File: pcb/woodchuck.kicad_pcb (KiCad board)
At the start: 2 copper layers, 34 parts, among them IC1 24AA01, IC101 ADP3335, IC201 u-blox_CAM-M8Q, IC601 MS5611-01BA03, J401 JSTA-4, P101 CONN_01X02, P401 SWD, P402 USB_OTG, SW401 SPST, U301 Radiometrix_MTX2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

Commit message: regenerated and imported netlist
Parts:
- added C405: 1u, Woodchuck:C0603, F.Cu at (199.6, 122.6)
- added C406: 4u7, Woodchuck:C0603, F.Cu at (191.8, 117.4)
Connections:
- U401 pad 11: (no net) -> Net-(R401-Pad2)
- U401 pad 14: Net-(R401-Pad2) -> /Radio/MTX2_TXD
- U401 pad 28: /Radio/MTX2_TXD -> (no net)
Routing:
- net /Radio/MTX2_TXD: track 0.00 -> 8.23 mm
- net Net-(R401-Pad2): track 10.1 -> 1.88 mm
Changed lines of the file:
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@@
 (kicad_pcb (version 4) (host pcbnew 4.0.2-4+6225~38~ubuntu14.04.1-stable)
   (general
-    (links 133)
-    (no_connects 34)
-    (area 150 99.125 225.000001 137.579762)
+    (links 137)
+    (no_connects 39)
+    (area 0 0 0 0)
     (thickness 1.6)
     (drawings 5)
     (tracks 374)
     (zones 0)
-    (modules 34)
+    (modules 36)
     (nets 38)
   )
@@
       (net 3 +3V3))
     (pad 10 smd rect (at 1.75 4.25 90) (size 0.3 1.2) (layers F.Cu F.Paste F.Mask))
-    (pad 11 smd rect (at 2.25 4.25 90) (size 0.3 1.2) (layers F.Cu F.Paste F.Mask))
+    (pad 11 smd rect (at 2.25 4.25 90) (size 0.3 1.2) (layers F.Cu F.Paste F.Mask)
+      (net 29 "Net-(R401-Pad2)"))
     (pad 12 smd rect (at 2.75 4.25 90) (size 0.3 1.2) (layers F.Cu F.Paste F.Mask)
       (net 35 /GPS/GPS_FROM_MCU))
@@
       (net 34 /GPS/GPS_TO_MCU))
     (pad 14 smd rect (at 4.25 2.25 90) (size 1.2 0.3) (layers F.Cu F.Paste F.Mask)
-      (net 29 "Net-(R401-Pad2)"))
+      (net 9 /Radio/MTX2_TXD))
     (pad 15 smd rect (at 4.25 1.75 90) (size 1.2 0.3) (layers F.Cu F.Paste F.Mask)
       (net 31 "Net-(R402-Pad2)"))
@@
     (pad 27 smd rect (at 1.75 -4.25 90) (size 0.3 1.2) (layers F.Cu F.Paste F.Mask)
       (net 10 /Radio/MTX2_P1))
-    (pad 28 smd rect (at 1.25 -4.25 90) (size 0.3 1.2) (layers F.Cu F.Paste F.Mask)
-      (net 9 /Radio/MTX2_TXD))
+    (pad 28 smd rect (at 1.25 -4.25 90) (size 0.3 1.2) (layers F.Cu F.Paste F.Mask))
     (pad 29 smd rect (at 0.75 -4.25 90) (size 0.3 1.2) (layers F.Cu F.Paste F.Mask))
     (pad 30 smd rect (at 0.25 -4.25 90) (size 0.3 1.2) (layers F.Cu F.Paste F.Mask)
@@
     (pad 2 smd rect (at 1.7 0 270) (size 0.8 1.7) (layers F.Cu F.Paste F.Mask)
       (net 3 +3V3))
+  )
+  (module Woodchuck:C0603 (layer F.Cu)
+    (at 199.64 122.58 90)
+    (fp_text reference C405 (at 0.7 -1.35 90) (layer F.SilkS) hide
+      (effects (font (size 1 1) (thickness 0.15)))
+    )
+    (fp_text value 1u (at 0.75 1.45 90) (layer F.SilkS)
+      (effects (font (size 1 1) (thickness 0.15)))
+    )
+    (fp_line (start -0.4 0.5) (end 2 0.5) (layer F.SilkS) (width 0.15))
+    (fp_line (start -0.4 -0.5) (end 2 -0.5) (layer F.SilkS) (width 0.15))
+    (pad 1 smd rect (at 0 0 90) (size 0.8 0.8) (layers F.Cu F.Paste F.Mask)
+      (net 3 +3V3))
+    (pad 2 smd rect (at 1.6 0 90) (size 0.8 0.8) (layers F.Cu F.Paste F.Mask)
+      (net 1 GND))
+  )
+  (module Woodchuck:C0603 (layer F.Cu)
+    (at 191.84 117.39 90)
+    (fp_text reference C406 (at 0.7 -1.35 90) (layer F.SilkS) hide
+      (effects (font (size 1 1) (thickness 0.15)))
+    )
+    (fp_text value 4u7 (at 0.75 1.45 90) (layer F.SilkS)
+      (effects (font (size 1 1) (thickness 0.15)))
+    )
+    (fp_line (start -0.4 0.5) (end 2 0.5) (layer F.SilkS) (width 0.15))
+    (fp_line (start -0.4 -0.5) (end 2 -0.5) (layer F.SilkS) (width 0.15))
+    (pad 1 smd rect (at 0 0 90) (size 0.8 0.8) (layers F.Cu F.Paste F.Mask)
+      (net 3 +3V3))
+    (pad 2 smd rect (at 1.6 0 90) (size 0.8 0.8) (layers F.Cu F.Paste F.Mask)
+      (net 1 GND))
   )
   (gr_line (start 180 100.35) (end 180.05 100.35) (angle 90) (layer F.SilkS) (width 0.2))
@@
   (segment (start 203.85 126.4) (end 202.2 126.4) (width 0.3) (layer F.Cu) (net 7))
   (segment (start 204.7 125.55) (end 203.85 126.4) (width 0.3) (layer F.Cu) (net 7))
+  (segment (start 201.55 117.9) (end 201.25 117.9) (width 0.3) (layer F.Cu) (net 9))
+  (segment (start 199.15 116.85) (end 199.15 117.7) (width 0.3) (layer F.Cu) (net 9))
+  (segment (start 200.9 117.55) (end 200 116.65) (width 0.3) (layer F.Cu) (net 9))
+  (segment (start 200 116.65) (end 199.35 116.65) (width 0.3) (layer F.Cu) (net 9))
+  (segment (start 199.35 116.65) (end 199.15 116.85) (width 0.3) (layer F.Cu) (net 9))
+  (segment (start 201.25 117.9) (end 200.9 117.55) (width 0.3) (layer F.Cu) (net 9))
+  (segment (start 202.65 119) (end 201.55 117.9) (width 0.3) (layer F.Cu) (net 9))
+  (segment (start 204.65 121) (end 202.65 119) (width 0.3) (layer F.Cu) (net 9))
   (segment (start 195.65 117.7) (end 195.65 118.76) (width 0.3) (layer F.Cu) (net 13))
   (segment (start 214.83 119.96) (end 215.92 121.05) (width 0.3) (layer F.Cu) (net 13))
@@
   (segment (start 207.375 121.9) (end 209.275 121.9) (width 0.3) (layer F.Cu) (net 28))
   (segment (start 209.275 121.9) (end 209.5 121.675) (width 0.3) (layer F.Cu) (net 28))
-  (segment (start 201.55 117.9) (end 201.25 117.9) (width 0.3) (layer F.Cu) (net 29))
   (segment (start 204.65 121.4) (end 204.65 121) (width 0.3) (layer F.Cu) (net 29))
   (segment (start 205.15 121.9) (end 204.65 121.4) (width 0.3) (layer F.Cu) (net 29))
   (segment (start 205.925 121.9) (end 205.15 121.9) (width 0.3) (layer F.Cu) (net 29))
-  (segment (start 202.65 119) (end 201.55 117.9) (width 0.3) (layer F.Cu) (net 29))
-  (segment (start 204.65 121) (end 202.65 119) (width 0.3) (layer F.Cu) (net 29))
-  (segment (start 199.15 116.85) (end 199.15 117.7) (width 0.3) (layer F.Cu) (net 29))
-  (segment (start 200.9 117.55) (end 200 116.65) (width 0.3) (layer F.Cu) (net 29))
-  (segment (start 200 116.65) (end 199.35 116.65) (width 0.3) (layer F.Cu) (net 29))
-  (segment (start 199.35 116.65) (end 199.15 116.85) (width 0.3) (layer F.Cu) (net 29))
-  (segment (start 201.25 117.9) (end 200.9 117.55) (width 0.3) (layer F.Cu) (net 29))
   (segment (start 207.375 120.45) (end 207.975 120.45) (width 0.3) (layer F.Cu) (net 30))
   (segment (start 207.975 120.45) (end 209.5 118.925) (width 0.3) (layer F.Cu) (net 30))

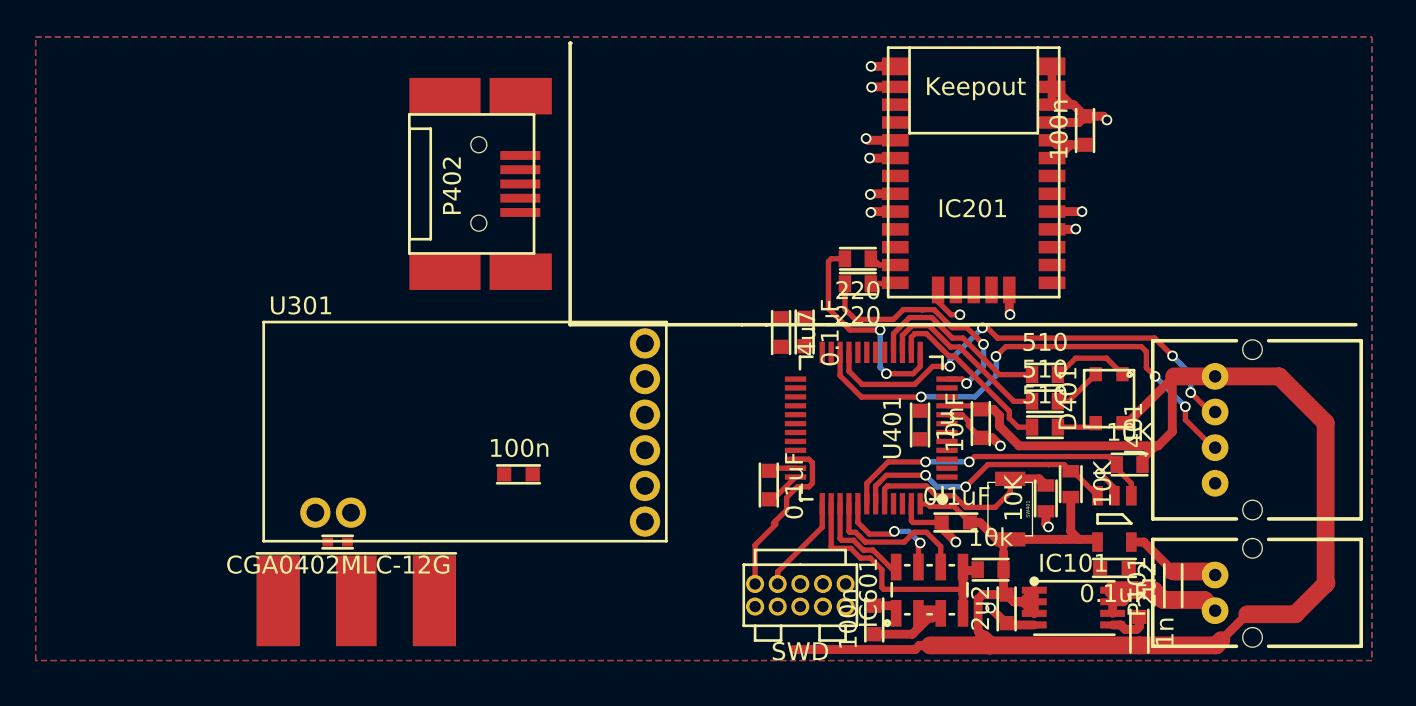
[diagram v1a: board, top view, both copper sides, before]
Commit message: PCB layout almost done. Add silkscreen and look over.
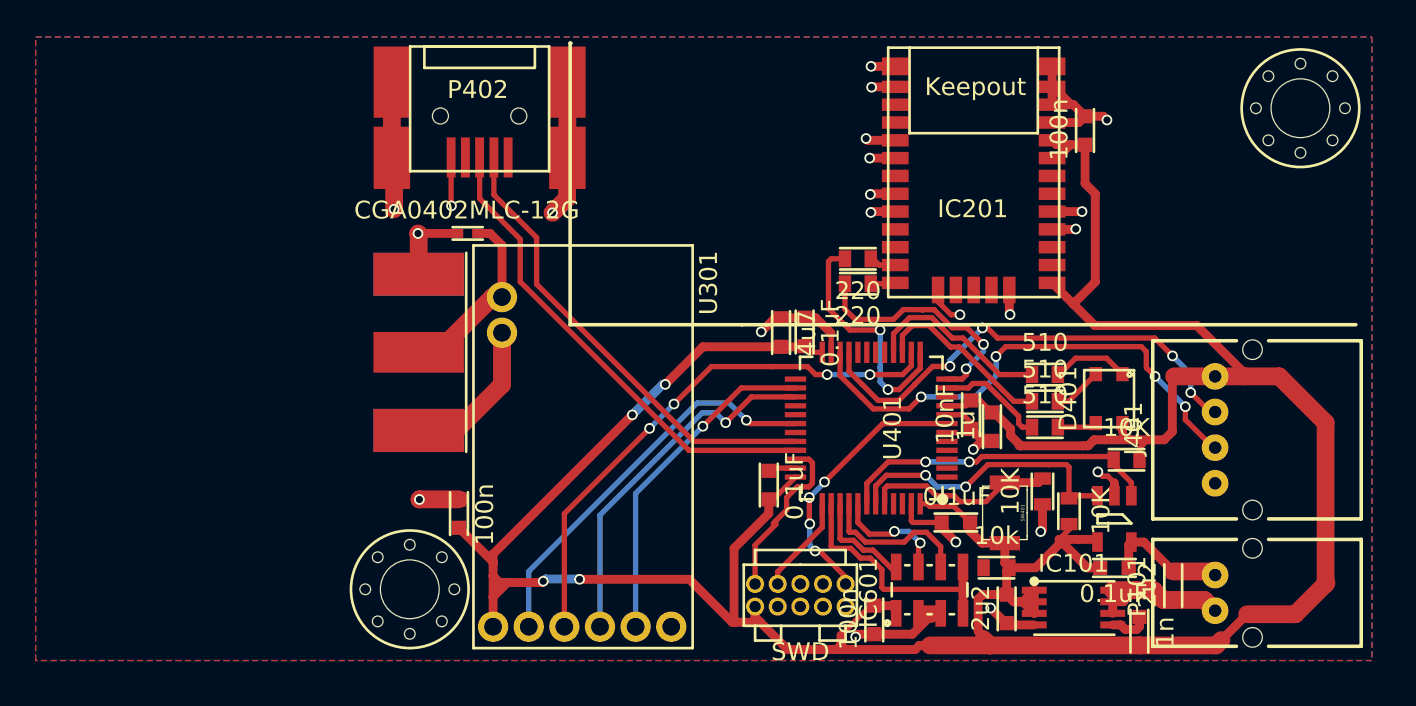
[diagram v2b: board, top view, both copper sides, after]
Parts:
- added X401: Mounting hole, Woodchuck:M3_MOUNT, F.Cu at (221.0, 104.0)
- added X402: Mounting hole, Woodchuck:M3_MOUNT, F.Cu at (171.0, 131.0)
- moved U301 20.4 mm to (174.6, 111.7), turned to 270 degrees
- moved D301 19.3 mm to (174.8, 111.0), turned to 180 degrees
- moved A301 14.4 mm to (171.5, 117.7), turned to 270 degrees
- moved C301 5.11 mm to (173.8, 127.5), turned to 90 degrees
- moved C405 4.31 mm to (203.7, 121.1), turned to 270 degrees
- moved R2 1.52 mm to (208.0, 126.6)
- moved C401 0.74 mm to (202.5, 120.4)
- moved P402 0.69 mm to (176.5, 106.8), turned to 270 degrees
- moved R404 0.43 mm to (206.5, 125.5)
- moved SW401 0.37 mm to (204.4, 126.7)
- moved R601 0.35 mm to (203.9, 129.8)
- moved R1 0.32 mm to (211.2, 123.7)
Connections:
- IC201 pad 2: (no net) -> Net-(IC201-Pad2)
- IC201 pad 28: (no net) -> Net-(IC201-Pad28)
- IC201 pad 29: (no net) -> Net-(IC201-Pad29)
- IC201 pad 3: (no net) -> Net-(IC201-Pad3)
- IC201 pad 30: (no net) -> Net-(IC201-Pad30)
- IC201 pad 6: (no net) -> Net-(IC201-Pad6)
- IC201 pad 7: (no net) -> Net-(IC201-Pad7)
- P401 pad 6: (no net) -> Net-(P401-Pad6)
- P401 pad 7: (no net) -> Net-(P401-Pad7)
- P401 pad 8: (no net) -> Net-(P401-Pad8)
- P402 pad 1: (no net) -> Net-(P402-Pad1)
- P402 pad 4: (no net) -> Net-(P402-Pad4)
- U401 pad 1: (no net) -> Net-(U401-Pad1)
- U401 pad 10: (no net) -> Net-(U401-Pad10)
- U401 pad 17: (no net) -> Net-(U401-Pad17)
- U401 pad 18: (no net) -> Net-(U401-Pad18)
- U401 pad 19: (no net) -> Net-(U401-Pad19)
- U401 pad 2: (no net) -> Net-(U401-Pad2)
- U401 pad 20: (no net) -> Net-(U401-Pad20)
- U401 pad 25: (no net) -> Net-(U401-Pad25)
- U401 pad 28: (no net) -> Net-(U401-Pad28)
- U401 pad 29: (no net) -> Net-(U401-Pad29)
- U401 pad 3: (no net) -> Net-(U401-Pad3)
- U401 pad 31: (no net) -> Net-(U401-Pad31)
- U401 pad 4: (no net) -> Net-(U401-Pad4)
- U401 pad 45: (no net) -> Net-(U401-Pad45)
- U401 pad 46: (no net) -> Net-(U401-Pad46)
- U401 pad 5: (no net) -> Net-(U401-Pad5)
- U401 pad 6: (no net) -> Net-(U401-Pad6)
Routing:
- net +3V3: track 107.3 -> 193.8 mm, vias 0 -> 4
- net GND: track 51.0 -> 94.1 mm, vias 16 -> 23
- net /microcontroller/USB_D+: track 0.00 -> 27.3 mm
- net /microcontroller/USB_D-: track 0.00 -> 26.3 mm
- net /Radio/MTX2_EN/PGM: track 0.00 -> 22.5 mm, vias 0 -> 1
- net /Radio/MTX2_TXD: track 8.23 -> 30.5 mm, vias 0 -> 4
- net /Radio/MTX2_P1: track 0.00 -> 20.4 mm, vias 0 -> 1
- net /Radio/MTX2_P0: track 0.00 -> 18.9 mm, vias 0 -> 1
- net /microcontroller/nRST: track 0.00 -> 15.3 mm, vias 0 -> 4
- net Net-(A301-Pad1): track 0.00 -> 10.5 mm
- net Net-(R401-Pad2): track 1.88 -> 6.13 mm
- net /GPS/GPS_TO_MCU: track 12.5 -> 13.8 mm
- net Net-(IC1-Pad3): track 15.3 -> 16.4 mm
- net /microcontroller/BOOT0: track 11.7 -> 10.7 mm
- net /barometer/BARO_CS: track 14.4 -> 13.6 mm
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
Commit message: Added logo and names to silk screen.
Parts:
- added X403: CUSF LOGO, Woodchuck:cusf_logo, F.Cu at (194.3, 109.7)
- added X404: CUSF LOGO BACK, Woodchuck:cusf_logo_full, F.Cu at (241.7, 98.8)
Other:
- board text added: "G Brooks E R Eide A Raghu B Wong J M Wood"
- board text added: "Woodchuck 1"

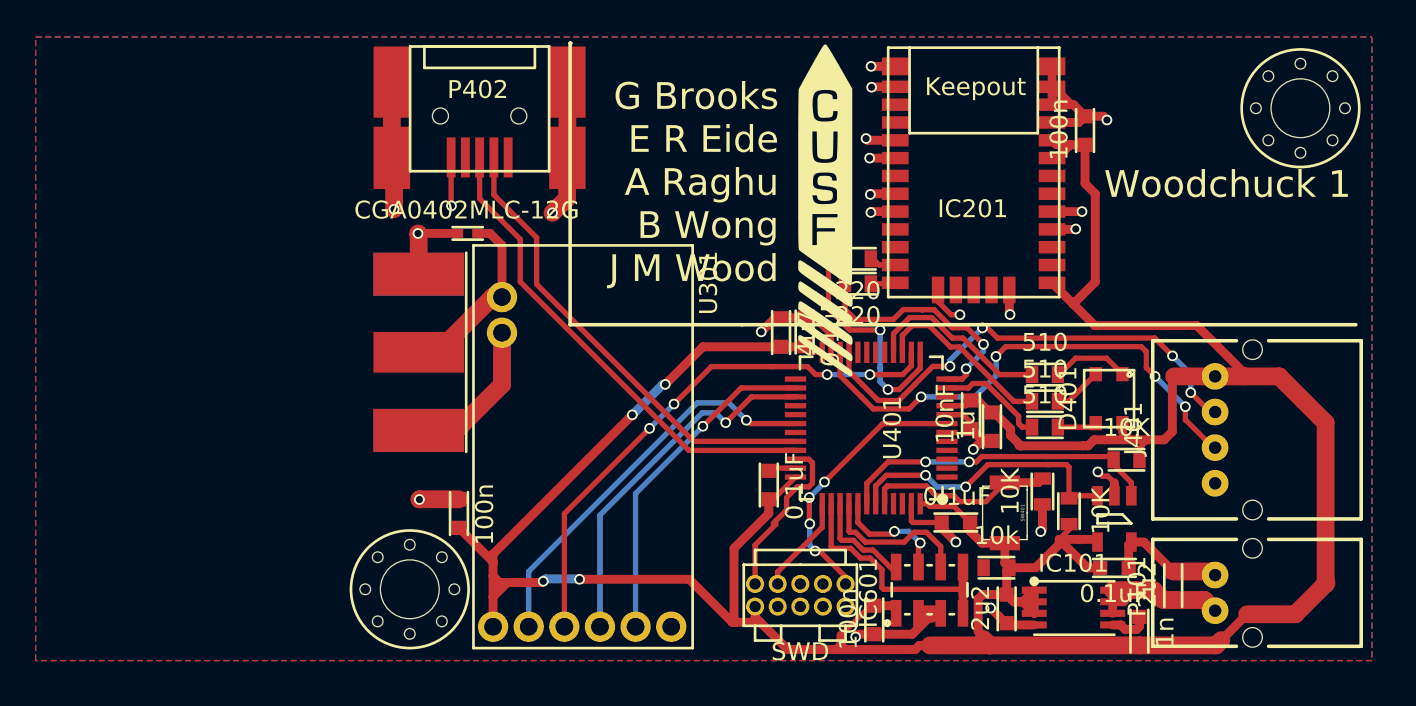
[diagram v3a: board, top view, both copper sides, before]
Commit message: Fixed edge cuts
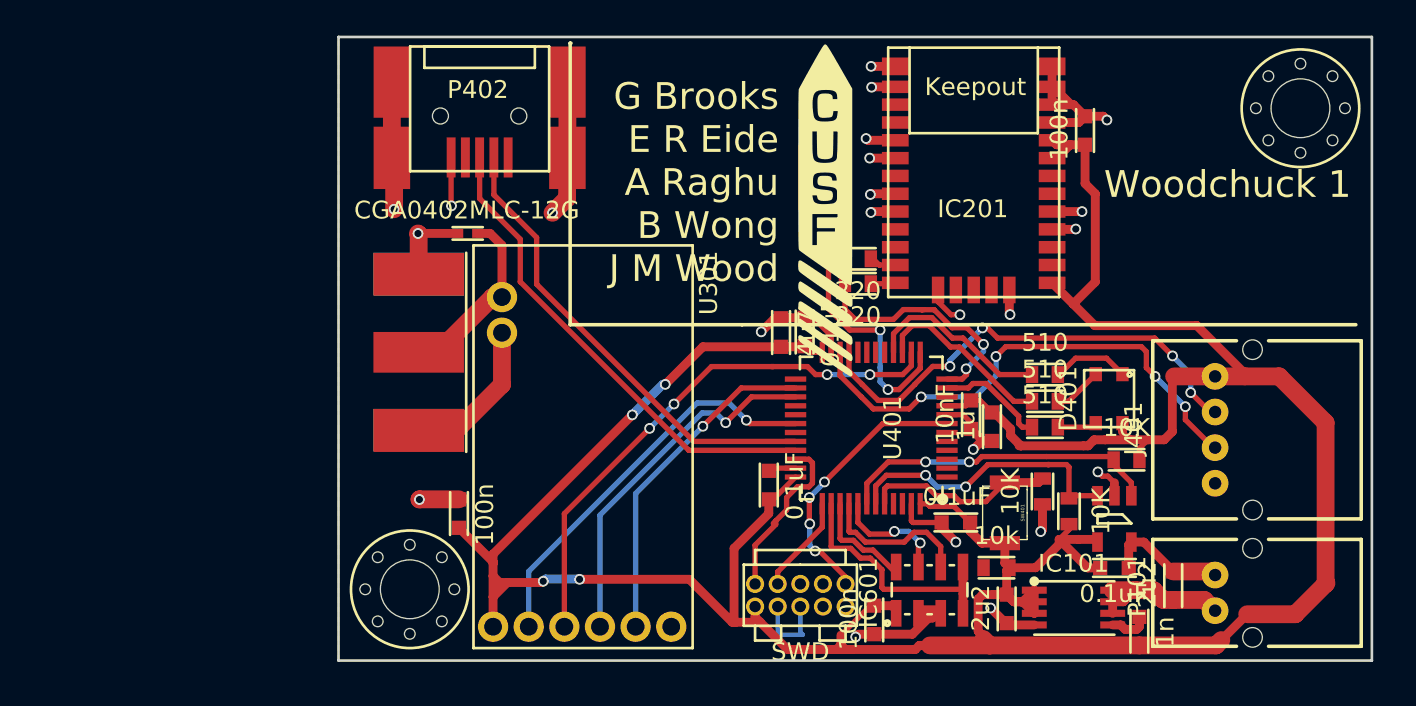
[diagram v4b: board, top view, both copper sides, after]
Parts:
- moved X404 50.8 mm to (196.0, 121.0)
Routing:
- net GND: track 94.1 -> 98.7 mm
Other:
- board outline added: 58 x 35 mm
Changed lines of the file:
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@@
   (general
     (links 137)
-    (no_connects 6)
+    (no_connects 4)
     (area 150 78.84134 263.521601 137.579762)
     (thickness 1.6)
-    (drawings 10)
-    (tracks 558)
+    (drawings 14)
+    (tracks 563)
     (zones 0)
     (modules 40)
@@
     (34 B.Paste user)
     (35 F.Paste user)
-    (36 B.SilkS user)
+    (36 B.SilkS user hide)
     (37 F.SilkS user)
     (38 B.Mask user)
@@
     (43 Eco2.User user)
     (44 Edge.Cuts user)
-    (45 Margin user)
+    (45 Margin user hide)
     (46 B.CrtYd user)
     (47 F.CrtYd user)
@@
   )
   (setup
-    (last_trace_width 0.3)
+    (last_trace_width 0.25)
     (user_trace_width 0.3)
     (user_trace_width 0.5)
@@
     (pad_drill 0.762)
     (pad_to_mask_clearance 0.2)
-    (aux_axis_origin 0 0)
-    (grid_origin 150 100)
+    (aux_axis_origin 167 135)
+    (grid_origin 167 135)
     (visible_elements 7FFCDFFF)
     (pcbplotparams
@@
   )
   (module Woodchuck:cusf_logo_full (layer F.Cu)
-    (at 241.68 98.85)
+    (at 196 121)
     (fp_text reference X404 (at 0 0) (layer B.SilkS) hide
       (effects (font (thickness 0.3)))
@@
       (xy 14.478 -10.583129) (xy 14.478 -10.583129)) (layer B.SilkS) (width 0.1))
   )
+  (gr_line (start 225 135) (end 167 135) (angle 90) (layer Edge.Cuts) (width 0.15))
+  (gr_line (start 225 100) (end 225 135) (angle 90) (layer Edge.Cuts) (width 0.15))
+  (gr_line (start 167 100) (end 225 100) (angle 90) (layer Edge.Cuts) (width 0.15))
+  (gr_line (start 167 135) (end 167 100) (angle 90) (layer Edge.Cuts) (width 0.15))
   (gr_text "Woodchuck 1" (at 216.9 108.28) (layer F.SilkS)
     (effects (font (size 1.5 1.5) (thickness 0.3)))
@@
   (gr_line (start 191.05 116.15) (end 189.65 116.15) (angle 90) (layer F.SilkS) (width 0.2))
   (gr_line (start 224.1 116.15) (end 191 116.15) (angle 90) (layer F.SilkS) (width 0.2))
+  (segment (start 191.65 131.97) (end 191.65 133.52) (width 0.25) (layer B.Cu) (net 1))
+  (segment (start 192.92 133.41) (end 192.92 131.97) (width 0.25) (layer B.Cu) (net 1))
+  (segment (start 193.06 133.55) (end 192.92 133.41) (width 0.25) (layer B.Cu) (net 1))
+  (segment (start 191.68 133.55) (end 193.06 133.55) (width 0.25) (layer B.Cu) (net 1))
+  (segment (start 191.65 133.52) (end 191.68 133.55) (width 0.25) (layer B.Cu) (net 1))
   (segment (start 206.51 126.235) (end 206.51 127.66) (width 0.5) (layer F.Cu) (net 1))
   (via (at 206.41 127.76) (size 0.6) (drill 0.4) (layers F.Cu B.Cu) (net 1))
@@
   (segment (start 197.75 124.6) (end 199.95 124.6) (width 0.3) (layer F.Cu) (net 37))
   (segment (start 197.15 125.2) (end 197.75 124.6) (width 0.3) (layer F.Cu) (net 37))
+  (zone (net 1) (net_name GND) (layer B.Cu) (hatch none 0.508)
+    (connect_pads (clearance 0.508))
+    (min_thickness 0.254)
+    (fill yes (arc_segments 16) (thermal_gap 0.508) (thermal_bridge_width 0.508))
+    (polygon
+      (pts
+        (xy 225 135) (xy 167 135) (xy 167 100) (xy 225 100) (xy 225 135)
+      )
+    )
+  )
   (zone (net 0) (net_name "") (layer F.Cu) (hatch edge 0.508)
     (connect_pads (clearance 0.508))
@@
     (polygon
       (pts
-        (xy 225 135) (xy 150 135) (xy 150 100) (xy 225 100) (xy 225 135)
+        (xy 225 135) (xy 167 135) (xy 167 100) (xy 225 100) (xy 225 135)
       )
     )
-  )
-  (zone (net 0) (net_name "") (layer Edge.Cuts) (hatch none 0.508)
-    (connect_pads (clearance 0.508))
-    (min_thickness 0.254)
-    (fill yes (arc_segments 16) (thermal_gap 0.508) (thermal_bridge_width 0.508))
-    (polygon
-      (pts
-        (xy 225 135) (xy 167.01008 135) (xy 167.01 135.01) (xy 167.01 135) (xy 150 135)
-        (xy 150 100) (xy 225 100) (xy 225 135)
-      )
-    )
-  )
-  (zone (net 1) (net_name GND) (layer B.Cu) (hatch none 0.508)
-    (connect_pads (clearance 0.508))
-    (min_thickness 0.254)
-    (fill yes (arc_segments 16) (thermal_gap 0.508) (thermal_bridge_width 0.508))
-    (polygon
-      (pts
-        (xy 225 135) (xy 150 135) (xy 150 100) (xy 225 100) (xy 225 135)
-      )
-    )
